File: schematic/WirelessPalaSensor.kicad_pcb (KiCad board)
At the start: 2 copper layers, 30.5 x 45.1 mm, 18 parts, among them P1 USB_OTG, P2 SERIAL_TX, P3 Palazzetti Connector, SW1 RESET, SW2 RESCUE_MODE, U1 LM1117-3.3, U2 ESP-12, U3 DS18B20, U4 MCP4151-50k, U5 MCP4151-5k

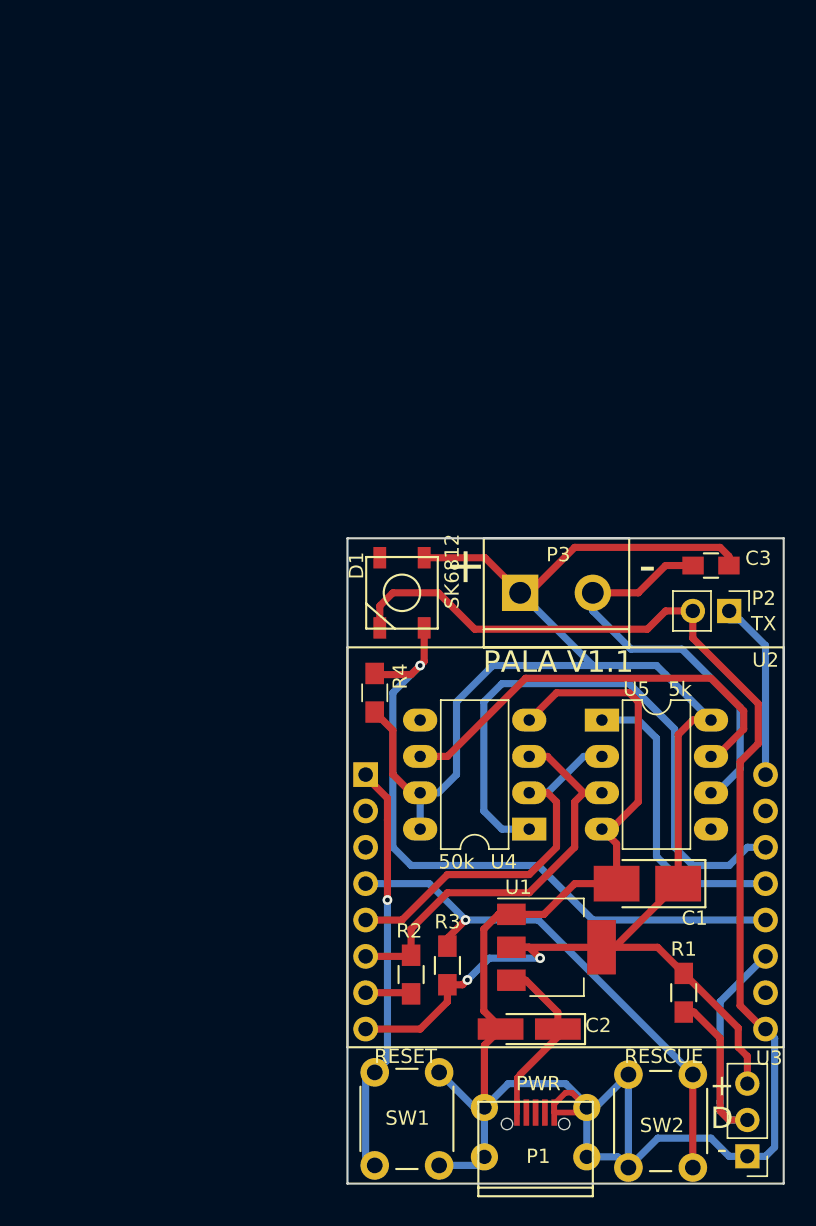
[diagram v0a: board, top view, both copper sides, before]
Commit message: Update Schematic to D1 Mini
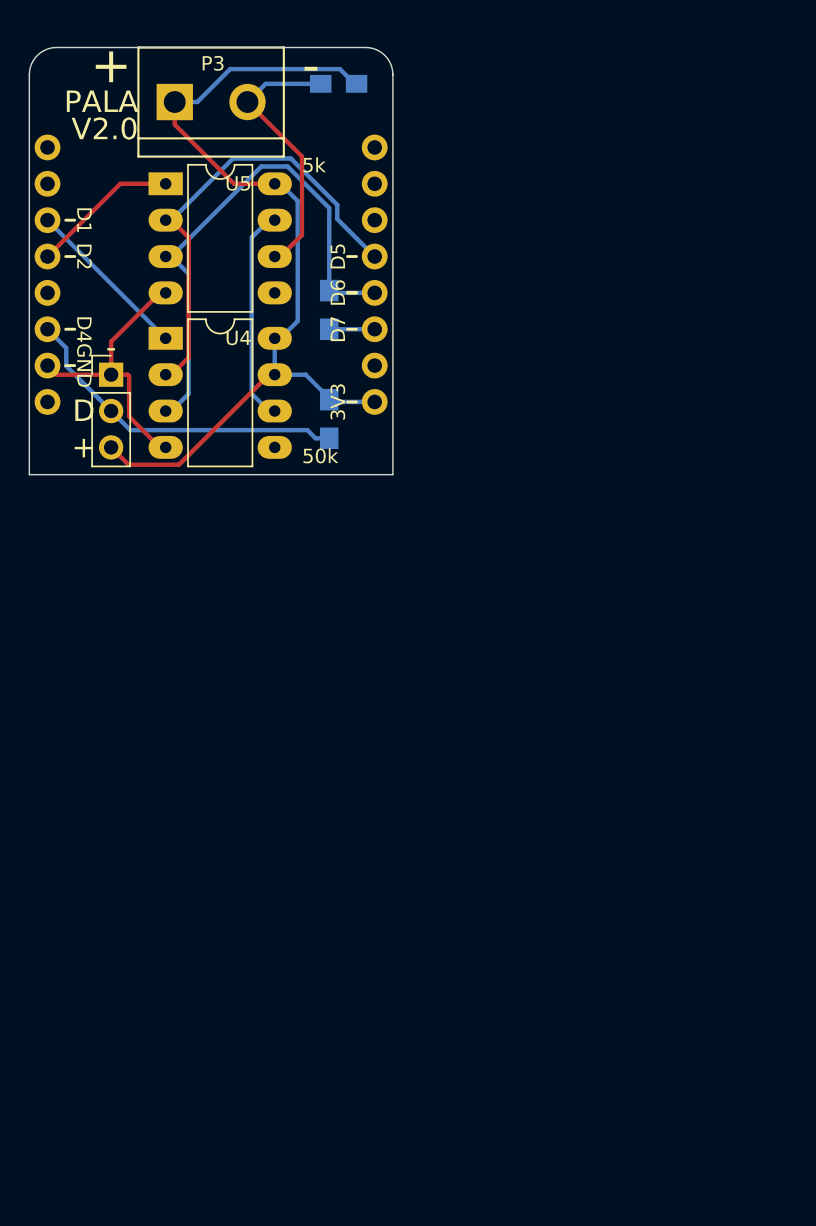
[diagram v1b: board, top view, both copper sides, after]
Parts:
- removed C1: 100uF, Capacitors_Tantalum_SMD:Tantalum_Case-B_EIA-3528-21_Hand
- removed C2: 10uF, Capacitors_Tantalum_SMD:Tantalum_Case-A_EIA-3216-18_Hand
- removed D1: SK6812, sk6812:Led_WS2812b
- removed P1: USB_OTG, MicroUSB:MicroUSB
- removed P2: SERIAL_TX, Pin_Headers:Pin_Header_Straight_1x02_Pitch2.54mm
- removed R3, R4: 10K, Resistors_SMD:R_0805_HandSoldering
- removed SW1: RESET, Buttons_Switches_ThroughHole:SW_PUSH_6mm
- removed SW2: RESCUE_MODE, Buttons_Switches_ThroughHole:SW_PUSH_6mm
- removed U2: ESP-12, ESP8266:ESP12WithAdapter
- C3, R1, R2: moved to B.Cu
- U1: value LM1117-3.3 -> WeMos_mini; footprint TO_SOT_Packages_SMD:SOT-223 -> wemos_d1_mini:wemos-d1-mini-DIL-only; moved to B.Cu
- moved U3 70.4 mm to (25.4, 45.1), turned to 0 degrees
- moved U1 52.8 mm to (32.4, 38.1), turned to 90 degrees
- moved U5 48.3 mm to (29.2, 31.8)
- moved R1 47.1 mm to (40.6, 48.2)
- moved R2 46.8 mm to (40.6, 40.6)
- moved U4 42.7 mm to (29.2, 42.5), turned to 0 degrees
- moved C3 42.5 mm to (41.3, 24.8)
- moved P3 41.9 mm to (32.4, 26.0)
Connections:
- U1 pad 1: GND -> (no net)
- U1 pad 2: VCC -> GND
- U1 pad 3: Net-(C2-Pad1) -> Net-(R1-Pad2)
- U4 pad 1: Net-(U2-Pad14) -> Net-(U1-Pad6)
- U4 pad 2: Net-(U2-Pad5) -> Net-(U1-Pad12)
- U5 pad 1: Net-(U2-Pad13) -> Net-(U1-Pad5)
- U5 pad 2: Net-(U2-Pad5) -> Net-(U1-Pad12)
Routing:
- net GND: track 168.4 -> 19.8 mm
- net VCC: track 130.0 -> 61.9 mm, vias 2 -> 0
- net Net-(D1-Pad4): track 47.8 -> 0.00 mm, vias 1 -> 0
- net Net-(U2-Pad14): track 42.2 -> 0.00 mm
- net Net-(R3-Pad1): track 37.2 -> 0.00 mm, vias 1 -> 0
- net Net-(U1-Pad12): track 0.00 -> 32.4 mm
- net Net-(SW1-Pad1): track 28.5 -> 0.00 mm, vias 1 -> 0
- net Net-(U2-Pad5): track 27.5 -> 0.00 mm
- net Net-(U2-Pad13): track 21.0 -> 0.00 mm
- net Net-(U4-Pad6): track 30.2 -> 15.1 mm
- net Net-(C2-Pad1): track 12.4 -> 0.00 mm
- net Net-(P2-Pad1): track 12.3 -> 0.00 mm
- net Net-(U1-Pad6): track 0.00 -> 11.7 mm
- net Net-(C3-Pad2): track 30.4 -> 19.0 mm
- net Net-(U1-Pad5): track 0.00 -> 10.4 mm
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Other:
- board size 30.5 x 45.1 mm -> 25.4 x 29.8 mm
- net class Default: clearance 0.3 -> 0.254; trace_width 0.5 -> 0.3048
- net class MicroUSB removed
- rule pad_to_mask_clearance: 0.2 -> 0.127
- rule trace_clearance: 0.3 -> 0.254
- board text added: "3V3"
- board text added: "D1"
- board text added: "D2"
- board text added: "D4"
- board text added: "D5"
- board text added: "D6"
- board text added: "D7"
- board text added: "GND"
- board text added: "PALA"
- board text added: "V2.0"
- board text removed: "PALA V1.1"
- board text removed: "PWR"
- board text removed: "RESCUE"
- board text removed: "RESET"
- board text removed: "TX"
- board text removed: "V1.1"
